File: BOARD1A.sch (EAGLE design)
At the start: 37 parts, among them U1 MCP23008

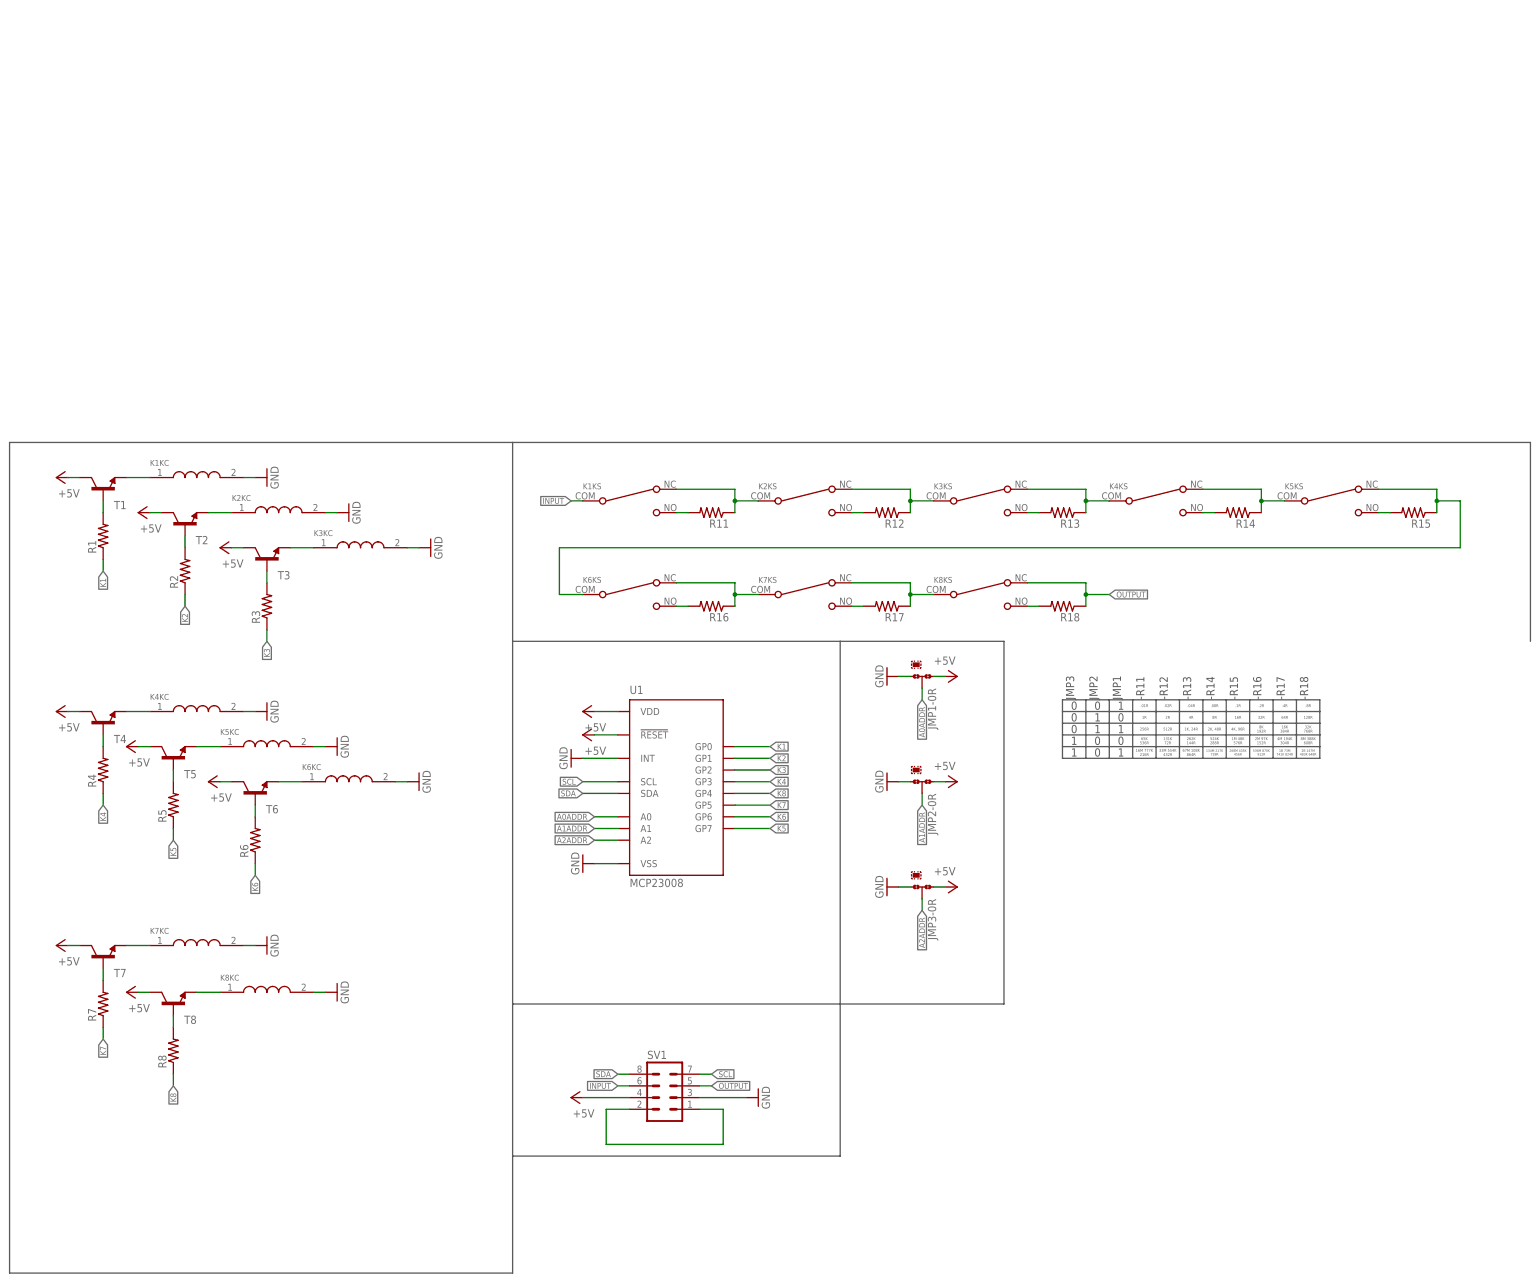
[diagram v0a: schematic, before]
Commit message: Changed Parts
Changed relay from 5VDC Coil to 12 VDC so it’s only 40mA. Changed to
SOT-23 SBT Transistor (100mA capability). removed bias resistors.
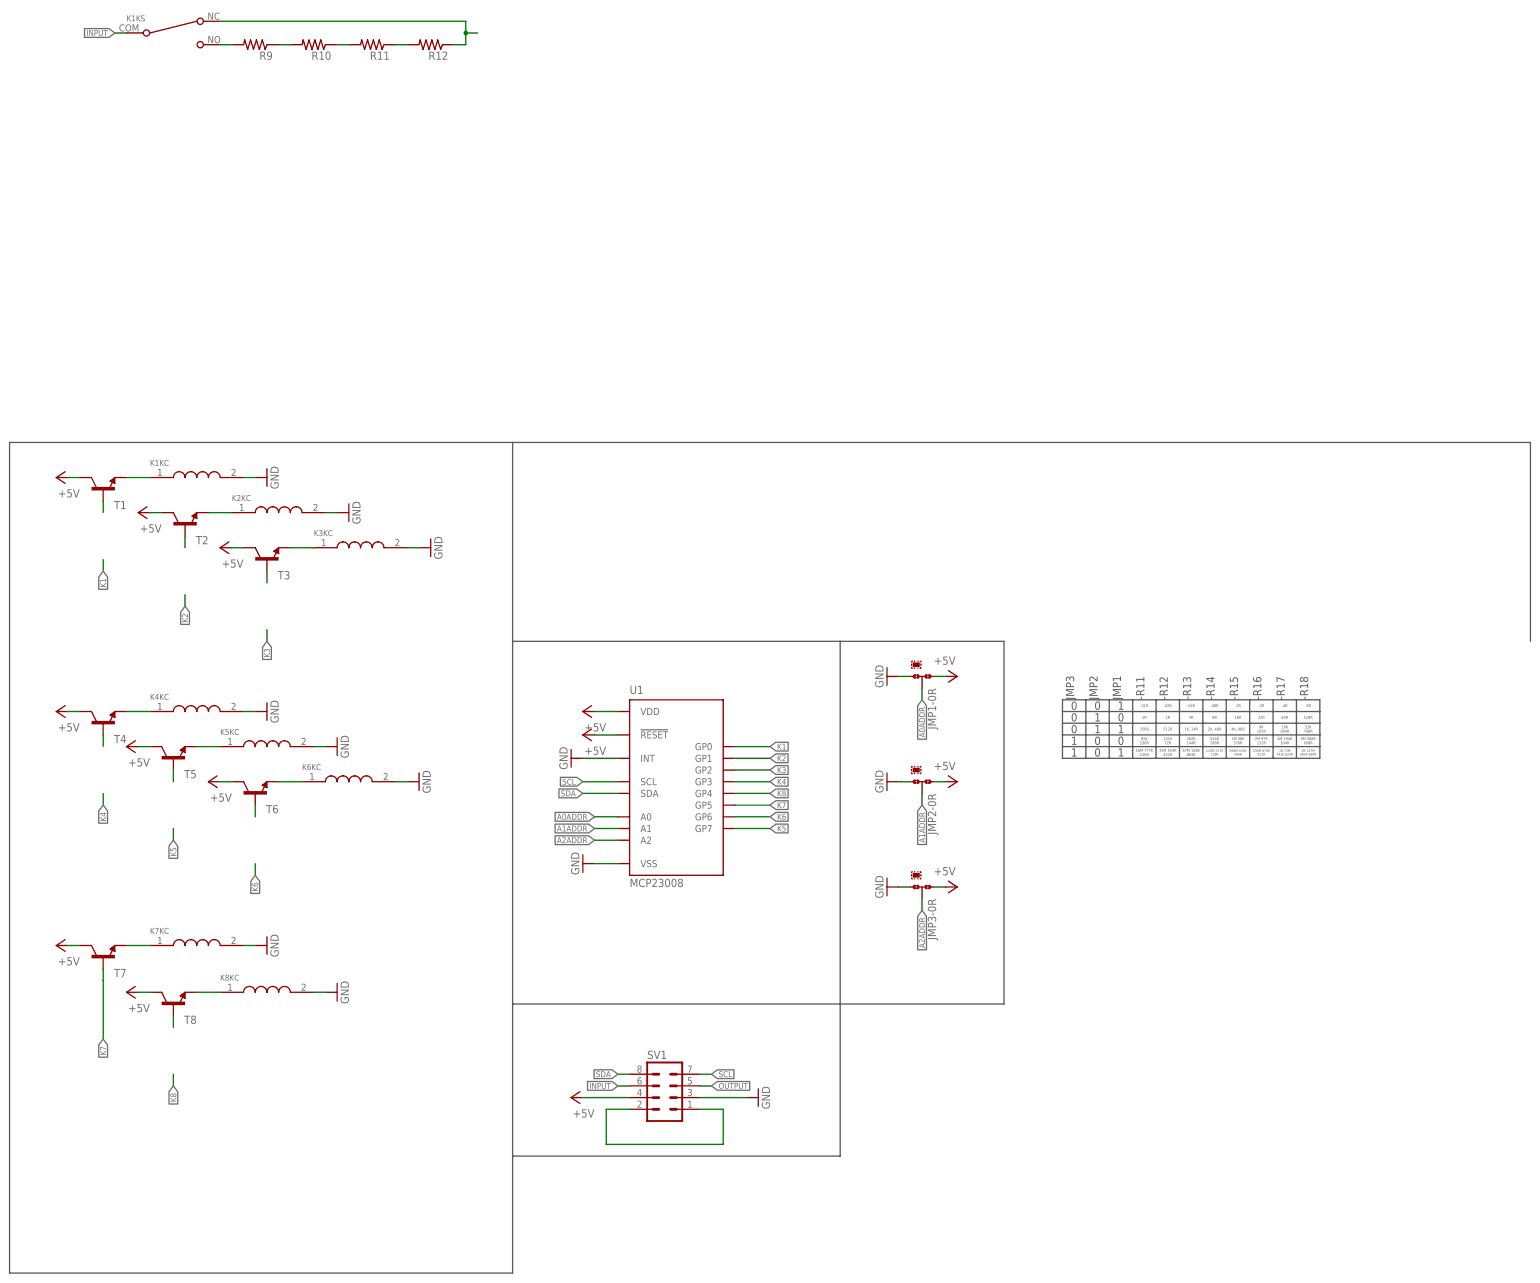
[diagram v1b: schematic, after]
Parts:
- removed R1, R2, R3, R4, R5, R6, R7, R8: (no value), resistor:R-US_M0805
- removed R13, R14, R15, R16, R17, R18: (no value), resistor:R-US_0207/12
- added R10, R9: (no value), resistor:R-US_0207/12
- K1: value (none) -> G5LE-1-VD DC12
- T1, T2, T3, T4, T5, T6, T7, T8: device transistor:-NPN-TO92-EBC -> transistor-neu-to92:MMUN2211LT1-NPN-SC59-BEC
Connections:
- removed net N$110: K1KS.P$NO, R11.2
- removed net N$111: K1KS.P$NC, K2KS.P$COM, R11.1
- removed net N$112: K2KS.P$NO, R12.2
- removed net N$113: K2KS.P$NC, K3KS.P$COM, R12.1
- removed net N$114: K3KS.P$NC, K4KS.P$COM, R13.1
- removed net N$115: K3KS.P$NO, R13.2
- removed net N$116: K4KS.P$NC, K5KS.P$COM, R14.1
- removed net N$117: K4KS.P$NO, R14.2
- removed net N$118: K5KS.P$NC, K6KS.P$COM, R15.1
- removed net N$119: K5KS.P$NO, R15.2
- net K1: no longer R1.1
- net K2: no longer R2.1
- net K3: no longer R3.1
- net K4: no longer R4.1
- net K5: no longer R5.1
- net K6: no longer R6.1
- net K7: no longer R7.1
- net K8: no longer R8.1
- net N$1: now also K1KS.P$NO, R9.2; no longer K6KS.P$NO, R16.2
- net N$12: no longer R1.2
- net N$14: no longer R2.2
- net N$16: no longer R3.2
- net N$18: no longer R4.2
- net N$2: now also R10.2, R9.1; no longer K6KS.P$NC, K7KS.P$COM, R16.1
- net N$20: no longer R5.2
- net N$22: no longer R6.2
- net N$24: no longer R7.2
- net N$26: no longer R8.2
- net N$3: now also R10.1, R11.2; no longer K7KS.P$NO, R17.2
- net N$4: now also R11.1, R12.2; no longer K7KS.P$NC, K8KS.P$COM, R17.1
- net N$6: now also K1KS.P$NC, R12.1; no longer K8KS.P$NO, R18.2
- net OUTPUT: no longer K8KS.P$NC, R18.1
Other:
- moved on the sheet: K1KS, R11, R12
